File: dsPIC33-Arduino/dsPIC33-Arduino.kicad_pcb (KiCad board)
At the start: 2 copper layers, 68.6 x 53.3 mm, 61 parts, among them CON1 BARREL_JACK, P1 Power, P10 PIN20, P11 PIN5, P12 PWR_IN, P13 PIN2, P14 Power Select, P15 I2C, P16 PIN19, P17 UART, P2 Analog, P3 Digital, P4 Digital, P5 CONN_1, P6 CONN_1, P7 CONN_1, P8 CONN_1, P9 USB_B, SW1 SW_PUSH, U1 FT230XS, U2 LM1117 3V3, U3 dsPIC33EVxxxGM102-I/SP, U4 74LVC1G32, U5 7805, Y1 Crystal

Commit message: wip
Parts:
- moved U4 0.51 mm to (135.0, 88.9)
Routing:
- net VCC: track 52.9 -> 50.1 mm
- net /PrgEn: track 3.45 -> 3.98 mm
- net Net-(D6-Pad1): track 4.49 -> 4.33 mm, vias 1 -> 0

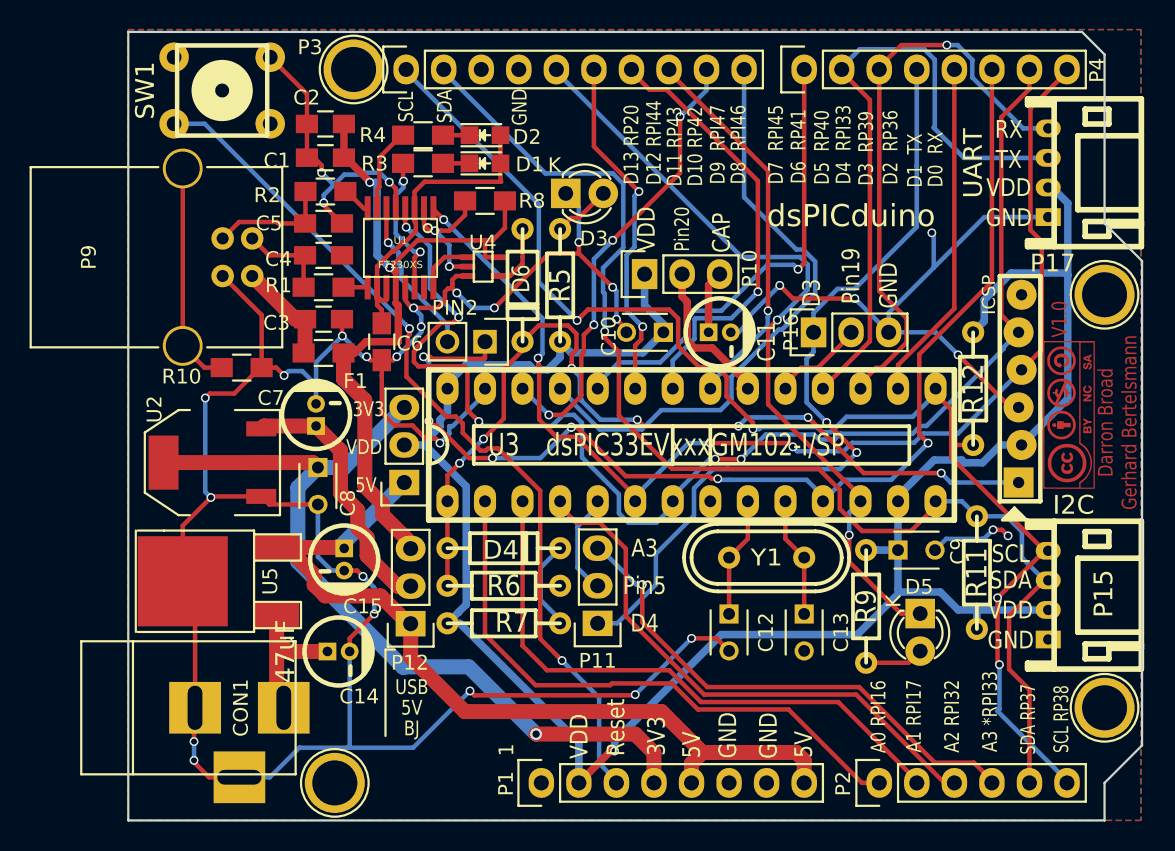
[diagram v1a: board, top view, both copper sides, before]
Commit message: optimize routing a little bit
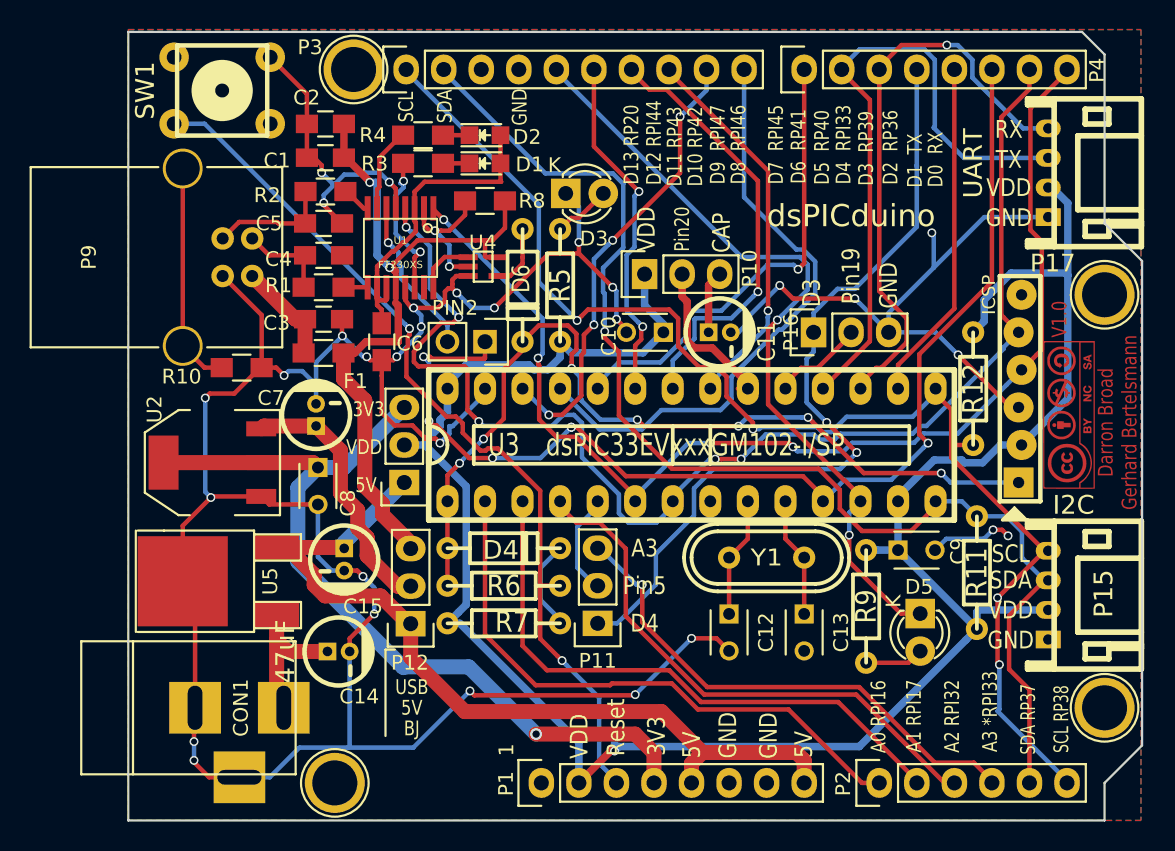
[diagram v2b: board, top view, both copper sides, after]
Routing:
- net VDD: track 143.3 -> 146.6 mm
- net /2: track 77.0 -> 77.3 mm, vias 7 -> 6
